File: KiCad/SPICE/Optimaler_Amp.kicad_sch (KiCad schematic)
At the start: 14 parts, among them U4 ${SIM.PARAMS}, U5 ${SIM.PARAMS}

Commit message: EQ Output Update
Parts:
- removed C33: 1 n, Capacitor_SMD:C_0805_2012Metric_Pad1.18x1.45mm_HandSolder, symbol Device:C_Small
- removed C37: 3n, Capacitor_SMD:C_0805_2012Metric_Pad1.18x1.45mm_HandSolder, symbol Device:C_Small
- removed R1, R2, R3: Potentiometer, symbol Simulation_SPICE:Potentiometer
- removed R58, R65: 33k, Resistor_SMD:R_0805_2012Metric_Pad1.20x1.40mm_HandSolder, symbol Device:R
- removed R76, R77: 6k8, Resistor_SMD:R_0805_2012Metric_Pad1.20x1.40mm_HandSolder, symbol Device:R
- added R24, R25, R33: 10k, Resistor_SMD:R_0805_2012Metric_Pad1.20x1.40mm_HandSolder, symbol Device:R
- added R32, R36: 6k8, Resistor_SMD:R_0805_2012Metric_Pad1.20x1.40mm_HandSolder, symbol Device:R
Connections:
- net GND: now also R36.1
- net In: now also U5.1 (+)
- net out: now also R25.2
- net at U4.1 (+): now also R32.2, R36.2
- net at U5.2 (-): now also R32.1, R33.1; no longer U5.5
- net at U4.2 (-): now also R24.2, R25.1
- new net: R24.1, R33.2, U5.5
- no-connect marks 1 -> 0
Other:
- moved on the sheet: U4, U5, V2

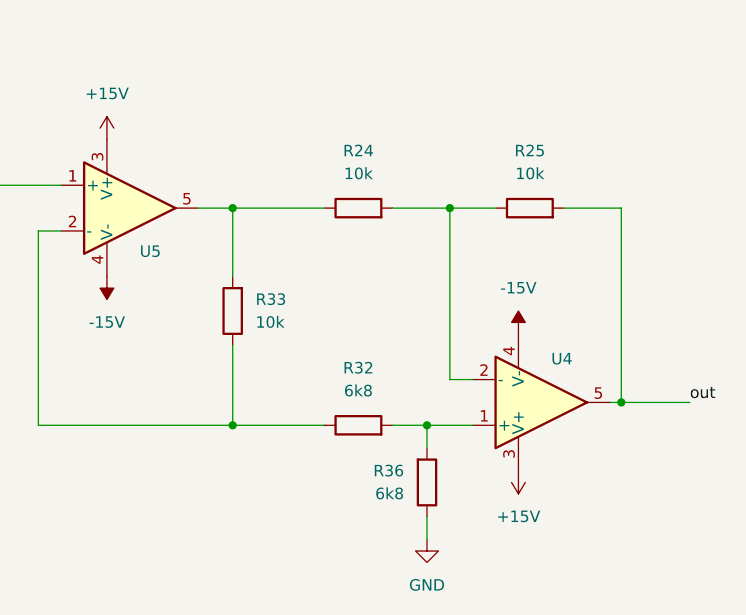
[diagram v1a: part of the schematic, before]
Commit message: Finales Update Ausgangsstufe
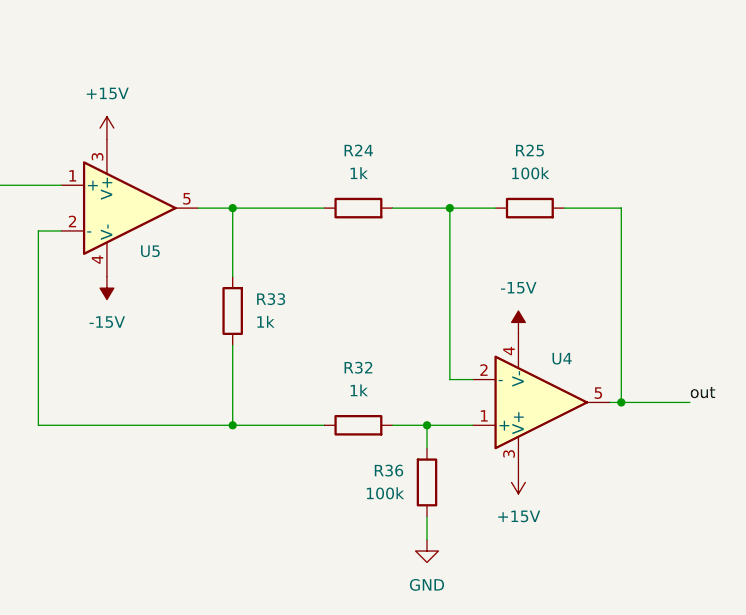
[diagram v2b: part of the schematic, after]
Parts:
- R24, R33: value 10k -> 1k
- R25: value 10k -> 100k
- R32: value 6k8 -> 1k
- R36: value 6k8 -> 100k
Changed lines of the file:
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@@
 			)
 		)
-		(property "Value" "10k"
+		(property "Value" "100k"
 			(at 179.07 81.28 90)
 			(show_name no)
@@
 			)
 		)
-		(property "Value" "10k"
+		(property "Value" "1k"
 			(at 160.02 81.28 90)
 			(show_name no)
@@
 			)
 		)
-		(property "Value" "6k8"
+		(property "Value" "100k"
 			(at 165.1 116.8399 0)
 			(show_name no)
@@
 			)
 		)
-		(property "Value" "10k"
+		(property "Value" "1k"
 			(at 148.59 97.7899 0)
 			(show_name no)
@@
 			)
 		)
-		(property "Value" "6k8"
+		(property "Value" "1k"
 			(at 160.02 105.41 90)
 			(show_name no)

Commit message: Update
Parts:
- R24: value 1k -> 10k
- R25: value 100k -> 47k
- R33: value 1k -> 50k
- R36: value 100k -> 15k
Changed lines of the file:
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@@
 			)
 		)
-		(property "Value" "100k"
+		(property "Value" "47k"
 			(at 179.07 81.28 90)
 			(show_name no)
@@
 			)
 		)
-		(property "Value" "1k"
+		(property "Value" "10k"
 			(at 160.02 81.28 90)
 			(show_name no)
@@
 			)
 		)
-		(property "Value" "100k"
+		(property "Value" "15k"
 			(at 165.1 116.8399 0)
 			(show_name no)
@@
 			)
 		)
-		(property "Value" "1k"
+		(property "Value" "50k"
 			(at 148.59 97.7899 0)
 			(show_name no)
